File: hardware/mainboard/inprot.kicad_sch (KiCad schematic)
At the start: 3 parts

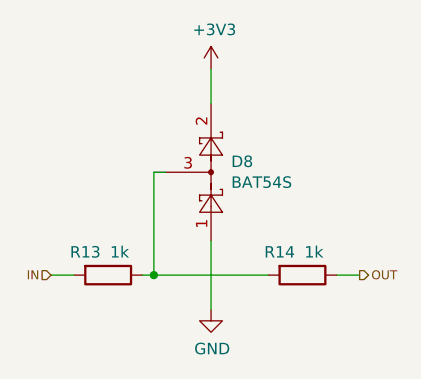
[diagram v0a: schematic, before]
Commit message: Mainboard routeado.
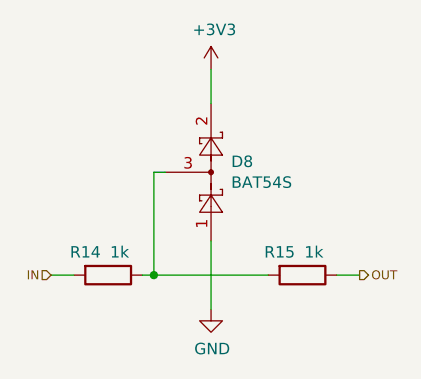
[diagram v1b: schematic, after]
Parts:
- renumbered R13 to R14, R14 to R15
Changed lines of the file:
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@@
   (symbol (lib_id "Device:R") (at 140.97 91.44 270) (unit 1)
     (in_bom yes) (on_board yes)
-    (property "Reference" "R13" (id 0) (at 138.43 88.9 90))
+    (property "Reference" "R14" (id 0) (at 138.43 88.9 90))
     (property "Value" "1k" (id 1) (at 142.24 88.9 90))
     (property "Footprint" "Resistor_SMD:R_1206_3216Metric" (id 2) (at 140.97 89.662 90)
@@
   (symbol (lib_id "Device:R") (at 162.56 91.44 270) (unit 1)
     (in_bom yes) (on_board yes)
-    (property "Reference" "R14" (id 0) (at 160.02 88.9 90))
+    (property "Reference" "R15" (id 0) (at 160.02 88.9 90))
     (property "Value" "1k" (id 1) (at 163.83 88.9 90))
     (property "Footprint" "Resistor_SMD:R_1206_3216Metric" (id 2) (at 162.56 89.662 90)
